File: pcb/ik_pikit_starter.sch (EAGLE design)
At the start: 30 parts, among them U1 QRE1113

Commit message: revised version
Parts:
- removed U$2: MCP9700SMD, SparkFun-Sensors:MCP9700SMD
- added U2: MCP9700SMD, Ai_IC:MCP9700SMD
- C1, C2: device rcl:C-EUC0805 -> Ai_Passives:CAP0805
- LOGO1: device SparkFun-Aesthetics:OSHW-LOGOS -> Ai_Miscellany:OSHW-LOGOS
- R1, R10, R11, R2, R3, R4, R5, R6, R7, R8, R9: device rcl:R-EU_R0805 -> Ai_Passives:RES0805
- U$1: value IHSAN_MCP3422 -> MCP3422; device SparkFun-DigitalIC_ihsan:IHSAN_MCP3422 -> Ai_IC:MCP3422
- U1: device SparkFun-Sensors:QRE1113 -> Ai_IC:QRE1113
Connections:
- net DISTANCE_SENSOR renamed D
- removed net TEMP_SENSOR: U$1.CH2+, U$2.VO
- new net T: U$1.CH2+, U2.VO
- net 3V3: now also U1.CO, U2.VCC; no longer U$2.VCC, U1.C
- net GND: now also U1.CA, U2.GND; no longer U$2.GND, U1.K
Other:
- moved on the sheet: C1, C2, S1

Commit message: adding values
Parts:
- removed U$1: MCP3422, Ai_IC:MCP3422
- added U3: MCP3422, Ai_IC:MCP3422
- C1, C2: value (none) -> 0.1uF
- LED1, LED2, LED3, LED4, LED5, LED6: value (none) -> BLUE
- R1: value (none) -> 100
- R10, R11, R3: value (none) -> 10K
- R2: value (none) -> 220
- R4, R5, R6, R7, R8, R9: value (none) -> 1K
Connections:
- net 3V3: now also U3.VDD; no longer U$1.VDD
- net D: now also U3.CH1+; no longer U$1.CH1+
- net GND: now also U3.CH1-, U3.CH2-, U3.GND; no longer U$1.CH1-, U$1.CH2-, U$1.GND
- net SCL: now also U3.SCL; no longer U$1.SCL
- net SDA: now also U3.SDA; no longer U$1.SDA
- net T: now also U3.CH2+; no longer U$1.CH2+
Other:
- moved on the sheet: C1, C2, I2C, JP1, LED1, LED2, LED3, LED4, LED5, LED6, POWER, R1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

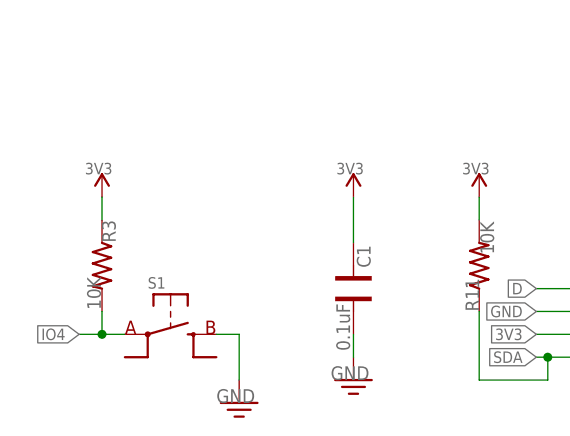
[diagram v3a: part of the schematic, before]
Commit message: fixed silkscreen
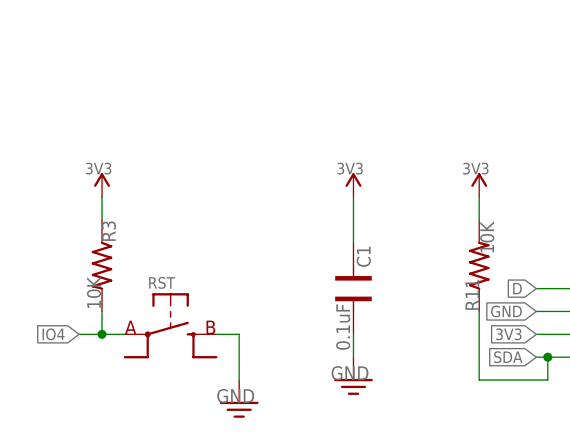
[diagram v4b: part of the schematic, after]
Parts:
- renumbered S1 to RST
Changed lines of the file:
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@@
 <part name="SUPPLY2" library="Ai_Power" deviceset="GND" device=""/>
 <part name="C2" library="Ai_Passives" deviceset="CAP" device="0805" value="0.1uF"/>
-<part name="S1" library="Ai_Electromechanical" deviceset="SW-SPST" device="SMD06X06" value="SW-SPSTSMD06X06"/>
+<part name="RST" library="Ai_Electromechanical" deviceset="SW-SPST" device="SMD06X06" value="SW-SPSTSMD06X06"/>
 <part name="R3" library="Ai_Passives" deviceset="RES" device="0805" value="10K"/>
 <part name="SUPPLY4" library="Ai_Power" deviceset="GND" device=""/>
@@
 <instance part="SUPPLY2" gate="GND" x="152.4" y="93.98"/>
 <instance part="C2" gate="G$1" x="137.16" y="128.27" rot="R180"/>
-<instance part="S1" gate="G$1" x="50.8" y="35.56"/>
+<instance part="RST" gate="G$1" x="50.8" y="35.56"/>
 <instance part="R3" gate="G$1" x="43.18" y="43.18" rot="R270"/>
 <instance part="SUPPLY4" gate="GND" x="58.42" y="27.94"/>
@@
 </segment>
 <segment>
-<pinref part="S1" gate="G$1" pin="B@1"/>
+<pinref part="RST" gate="G$1" pin="B@1"/>
 <wire x1="55.88" y1="35.56" x2="58.42" y2="35.56" width="0.1524" layer="91"/>
 <wire x1="58.42" y1="35.56" x2="58.42" y2="30.48" width="0.1524" layer="91"/>
@@
 </segment>
 <segment>
-<pinref part="S1" gate="G$1" pin="A@1"/>
+<pinref part="RST" gate="G$1" pin="A@1"/>
 <wire x1="45.72" y1="35.56" x2="43.18" y2="35.56" width="0.1524" layer="91"/>
 <pinref part="R3" gate="G$1" pin="2"/>
@@
 </sheet>
 </sheets>
-<errors>
-</errors>
 </schematic>
 </drawing>
